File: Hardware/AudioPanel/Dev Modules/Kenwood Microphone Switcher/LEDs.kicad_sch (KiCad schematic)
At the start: 15 parts

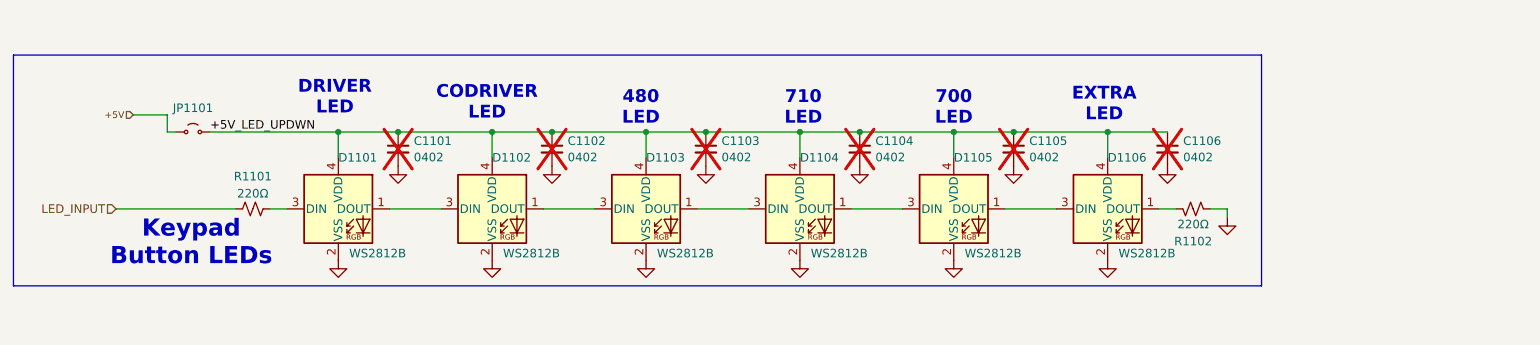
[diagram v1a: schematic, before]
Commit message: Added labeling and organized pages
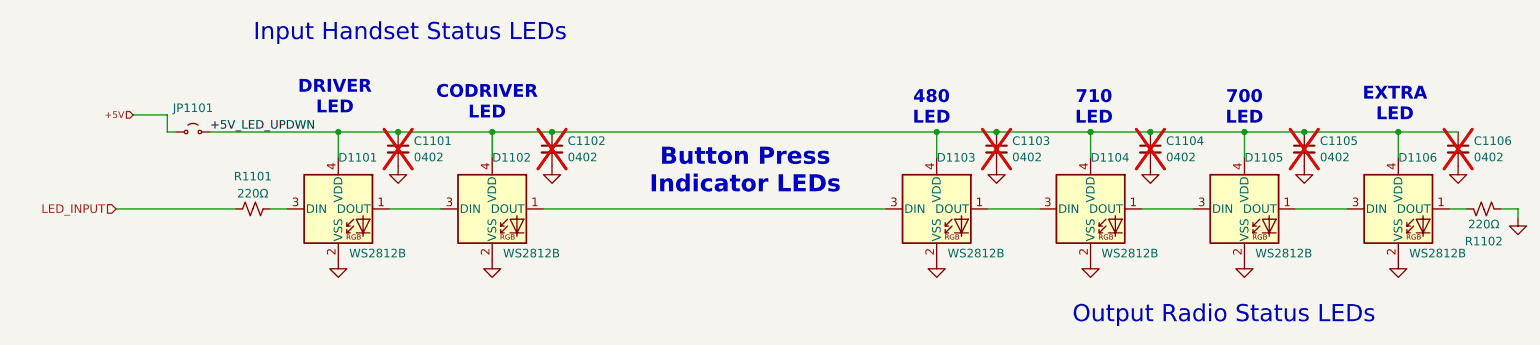
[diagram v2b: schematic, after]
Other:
- note added: "Button Press Indicator LEDs"
- note added: "Input Handset Status LEDs"
- note added: "Output Radio Status LEDs"
- note removed: "Keypad Button LEDs"
- company: (none) -> Thomas Francois - KX∅STL
- title: (none) -> Kenwood Handset Switcher - Multicolor LEDs
- moved on the sheet: C1103, C1104, C1105, C1106, D1103, D1104, D1105, D1106, R1102
